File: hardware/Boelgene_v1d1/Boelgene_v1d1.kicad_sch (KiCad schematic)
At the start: 68 parts, among them J1 batt, J2 pressure3, J3 pressure2, J4 pressure1, J5 pressure4, U1 Pico, U2 MCP3008, U3 PT8211-pt8211

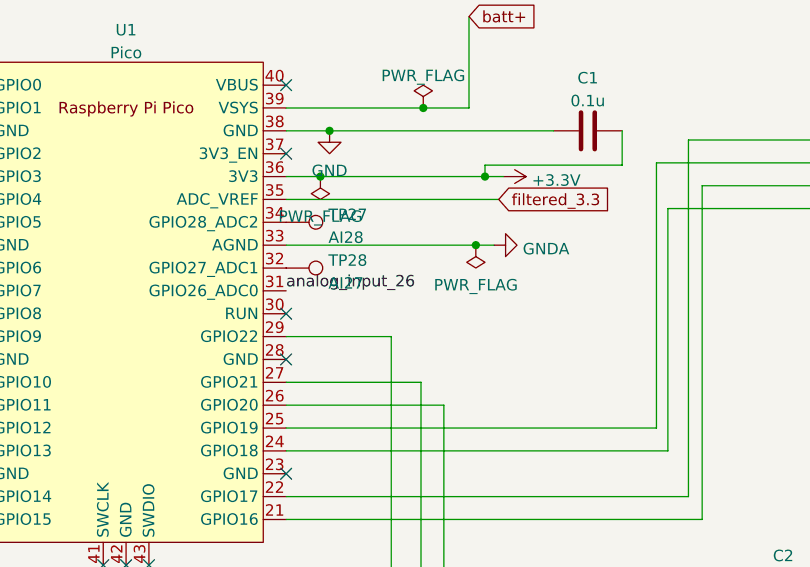
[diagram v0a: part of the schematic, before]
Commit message: Added correct ribbon input reference
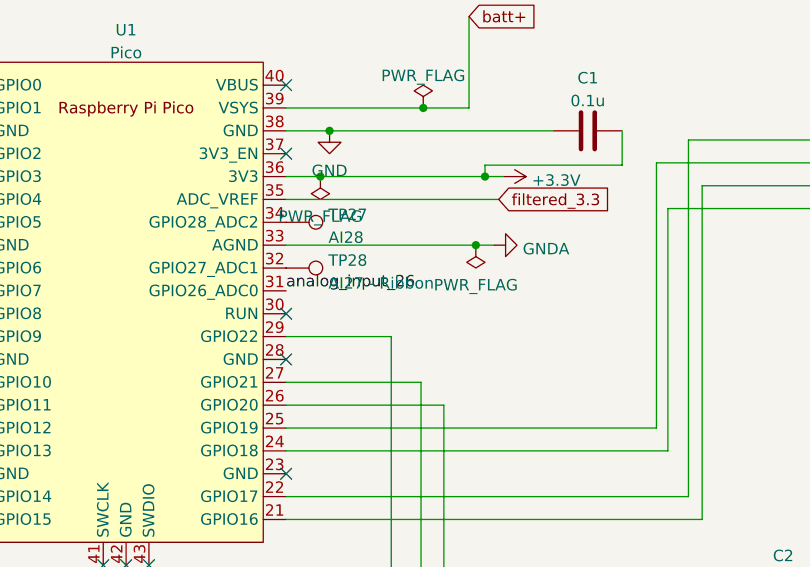
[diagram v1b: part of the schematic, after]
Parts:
- TP28: value AI27 -> AI27 - Ribbon
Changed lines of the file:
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@@
       (effects (font (size 1.27 1.27)) (justify left))
     )
-    (property "Value" "AI27" (id 1) (at 134.239 78.1562 90)
+    (property "Value" "AI27 - Ribbon" (id 1) (at 134.239 78.1562 90)
       (effects (font (size 1.27 1.27)) (justify left))
     )
@@
     )
     (path "/082ed3f3-5b9a-4eac-8ff0-91efa9ced314"
-      (reference "TP28") (unit 1) (value "AI27") (footprint "TestPoint:TestPoint_THTPad_2.0x2.0mm_Drill1.0mm")
+      (reference "TP28") (unit 1) (value "AI27 - Ribbon") (footprint "TestPoint:TestPoint_THTPad_2.0x2.0mm_Drill1.0mm")
     )
     (path "/f008859b-5d8e-4290-b5ee-6e6160db2859"

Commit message: Updated PCB with connectors
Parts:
- removed TP1, TP5, TP6: GND, TestPoint:TestPoint_THTPad_2.0x2.0mm_Drill1.0mm, symbol Connector:TestPoint
- removed TP11, TP2, TP4, TP9: ADC_ref, TestPoint:TestPoint_THTPad_2.0x2.0mm_Drill1.0mm, symbol Connector:TestPoint
- removed TP14: Ref+, TestPoint:TestPoint_THTPad_2.0x2.0mm_Drill1.0mm, symbol Connector:TestPoint
- removed TP15: D4, TestPoint:TestPoint_THTPad_2.0x2.0mm_Drill1.0mm, symbol Connector:TestPoint
- removed TP16: D5, TestPoint:TestPoint_THTPad_2.0x2.0mm_Drill1.0mm, symbol Connector:TestPoint
- removed TP17: LED, TestPoint:TestPoint_THTPad_2.0x2.0mm_Drill1.0mm, symbol Connector:TestPoint
- removed TP18: Ref-, TestPoint:TestPoint_THTPad_2.0x2.0mm_Drill1.0mm, symbol Connector:TestPoint
- removed TP19: Oct+, TestPoint:TestPoint_THTPad_2.0x2.0mm_Drill1.0mm, symbol Connector:TestPoint
- removed TP20: Oct-, TestPoint:TestPoint_THTPad_2.0x2.0mm_Drill1.0mm, symbol Connector:TestPoint
- removed TP21, TP22, TP24, TP26: GNDA, TestPoint:TestPoint_THTPad_2.0x2.0mm_Drill1.0mm, symbol Connector:TestPoint
- removed TP27: AI28, TestPoint:TestPoint_THTPad_2.0x2.0mm_Drill1.0mm, symbol Connector:TestPoint
- removed TP28: AI27 - Ribbon, TestPoint:TestPoint_THTPad_2.0x2.0mm_Drill1.0mm, symbol Connector:TestPoint
- removed TP32: pot5, TestPoint:TestPoint_THTPad_2.0x2.0mm_Drill1.0mm, symbol Connector:TestPoint
- removed TP33: pot4, TestPoint:TestPoint_THTPad_2.0x2.0mm_Drill1.0mm, symbol Connector:TestPoint
- removed TP34: pot3, TestPoint:TestPoint_THTPad_2.0x2.0mm_Drill1.0mm, symbol Connector:TestPoint
- removed TP35: pot2, TestPoint:TestPoint_THTPad_2.0x2.0mm_Drill1.0mm, symbol Connector:TestPoint
- removed TP36: pot1, TestPoint:TestPoint_THTPad_2.0x2.0mm_Drill1.0mm, symbol Connector:TestPoint
- removed TP44: out_dac1, TestPoint:TestPoint_THTPad_2.0x2.0mm_Drill1.0mm, symbol Connector:TestPoint
- removed TP45: out_dac2, TestPoint:TestPoint_THTPad_2.0x2.0mm_Drill1.0mm, symbol Connector:TestPoint
- added J10: Right, Connector_JST:JST_XH_B2B-XH-A_1x02_P2.50mm_Vertical, symbol Connector:Conn_01x02_Female
- added J11: Left (mono), Connector_JST:JST_XH_B2B-XH-A_1x02_P2.50mm_Vertical, symbol Connector:Conn_01x02_Female
- added J12: pots, Connector_JST:JST_PH_B6B-PH-K_1x06_P2.00mm_Vertical, symbol Connector:Conn_01x06_Female
- added J13: pots - power, Connector_JST:JST_XH_B2B-XH-A_1x02_P2.50mm_Vertical, symbol Connector:Conn_01x02_Female
- added J6: R ref+ // Y ref-, Connector_JST:JST_PH_B3B-PH-K_1x03_P2.00mm_Vertical, symbol Connector:Conn_01x03_Female
- added J7: LED // R- // W0 // Y+, Connector_JST:JST_PH_B4B-PH-K_1x04_P2.00mm_Vertical, symbol Connector:Conn_01x04_Female
- added J8: Y oct- // R oct+, Connector_JST:JST_PH_B3B-PH-K_1x03_P2.00mm_Vertical, symbol Connector:Conn_01x03_Female
- added J9: Ribbon, Connector_JST:JST_PH_B3B-PH-K_1x03_P2.00mm_Vertical, symbol Connector:Conn_01x03_Female
- added R4, R5: 220, Resistor_THT:R_Axial_DIN0207_L6.3mm_D2.5mm_P7.62mm_Horizontal, symbol Device:R
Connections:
- net GND: now also U2.9 (DGND), J6.2 (Pin_2), J7.1 (Pin_1), J8.2 (Pin_2)
- net GNDA: now also J10.1 (Pin_1), J11.1 (Pin_1), J13.1 (Pin_1), J9.2 (Pin_2); no longer U2.9 (DGND)
- net filtered_3.3: now also J13.2 (Pin_2), J9.3 (Pin_3)
- net at U1.32 (GPIO27_ADC1): now also J9.1 (Pin_1)
- net at C11.1: now also J11.2 (Pin_2)
- net at U1.11 (GPIO8): now also J8.3 (Pin_3)
- net at U1.10 (GPIO7): now also J6.1 (Pin_1)
- net at U1.12 (GPIO9): now also J8.1 (Pin_1)
- net analog_input_28: now reaches U1.34 (GPIO28_ADC2)
- net analog_input_28: now also J12.6 (Pin_6)
- net at U1.5 (GPIO3): now also J6.3 (Pin_3)
- net at U1.6 (GPIO4): now also R5.2
- net at U1.7 (GPIO5): now also R4.2
- net at U2.4 (CH3): now also J12.1 (Pin_1)
- net at U2.6 (CH5): now also J12.3 (Pin_3)
- net at C12.1: now also J10.2 (Pin_2)
- net at U2.5 (CH4): now also J12.2 (Pin_2)
- net at R3.1: now also J7.3 (Pin_3)
- net at U2.7 (CH6): now also J12.4 (Pin_4)
- net at U2.8 (CH7): now also J12.5 (Pin_5)
- new net: J7.4 (Pin_4), R5.1
- new net: J7.2 (Pin_2), R4.1
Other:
- moved on the sheet: C1, R3, TP13

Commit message: Updated PCB
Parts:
- U1: footprint Pico:RPi_Pico_SMD_TH -> Pico:RPi_Pico_TH
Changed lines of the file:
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@@
     (property "Reference" "U1" (id 0) (at 111.76 50.0212 0))
     (property "Value" "Pico" (id 1) (at 111.76 52.5581 0))
-    (property "Footprint" "Pico:RPi_Pico_SMD_TH" (id 2) (at 111.76 80.264 90)
+    (property "Footprint" "Pico:RPi_Pico_TH" (id 2) (at 111.76 80.264 90)
       (effects (font (size 1.27 1.27)) hide)
     )
@@
     )
     (path "/55d1c3b5-14d5-42c0-8335-6c6a74763122"
-      (reference "U1") (unit 1) (value "Pico") (footprint "Pico:RPi_Pico_SMD_TH")
+      (reference "U1") (unit 1) (value "Pico") (footprint "Pico:RPi_Pico_TH")
     )
     (path "/d8decf76-7406-4b5d-a4e7-b9a6ec9da4e3"
